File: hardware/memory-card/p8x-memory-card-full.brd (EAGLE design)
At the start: 160 x 100 mm, 30 parts, among them J1 FABC96R, U1 28C256, U2 62256, U3 74HCT245, U4 74HCT30, U5 74HCT138, U6 74HCT138, U7 74HCT00, U8 74HCT32, U9 74HCT08

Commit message: feat(hardware): use con-vg DIN 41612 footprints (MABC96R card / FABC96S backplane)
Replace the hand-rolled DIN96/DIN96C connector packages with the real Eagle
con-vg DIN 41612 footprints (geometry baked into the generator so it stays
self-contained): card edge = MABC96R (male right-angle), backplane = FABC96S
(female vertical) — both A/B/C @ 2.54mm, drill 0.9144, two M2.5 mounting holes
at y=+/-45. Card value -> MABC96R; pin->pad names unchanged (A1..C32) so the
netlist is intact.

con-vg centres the pad field on the element origin, so the backplane (hand-
placed/routed) was re-derived: slots dropped to y=54.6 to centre the pin field
on the 109mm board (pads now on-board), bus traces re-routed to the new A/B/C
columns (element at sx(i)-2.54). Cards auto-adapt via fp_box. All 8 boards
validate (0 errors).

Known: 3 placement-overlap WARNINGS on the backplane (power-LED resistor; CT2/RT1
clock terminators, both DNP) where the taller connector crowds the top/bottom
strips — to clear during the Fusion placement pass.

Co-Authored-By: Claude Opus 4.8 <noreply@anthropic.com>
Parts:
- J1: value FABC96R -> MABC96R; device p8x:DIN96C -> p8x:MABC96R
- moved J1 37.5 mm to (7.94, 49.6)

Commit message: feat(hardware): 100nF bypass caps to 0.1" lead pitch on all boards
The 100nF ceramic-disc decoupling/bypass caps used the shared C_DISC footprint
at 0.2" (5.08mm) lead spacing. The parts being sourced are 0.1" (2.54mm) pitch,
so retarget just those caps:

- Add a C_DISC1 footprint (pad 2 at y=-2.54) and a CAP1 device that reuses the
  CAP schematic symbol art but points at C_DISC1.
- Route the 100nF parts to CAP1: per-IC decoupling (CDn), the placement-flow
  copies, and the backplane per-slot caps C1-C10.
- Leave C_DISC (0.2") for the parts that still use it: the 1uF caps, the 150pF
  clock terminators (CT1/CT2), and the XTAL32 placeholder.

Regenerated all 8 boards (.sch/.brd/-full.brd) and the schematic PDFs; the
narrower pad field also relieves the backplane connector clearance. Validation:
0 errors on all boards.

Co-Authored-By: Claude Opus 4.8 <noreply@anthropic.com>
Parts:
- CD1, CD2, CD3, CD4, CD5, CD6, CD7, CD8, CD9: device p8x:C_DISC -> p8x:C_DISC1
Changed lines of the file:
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@@
 <attribute name="VALUE" x="17.87" y="92.66" size="1.778" layer="27" ratio="10"/>
 </element>
-<element name="CD1" library="p8x" package="C_DISC" value="100N" x="37.41" y="95.10" smashed="yes">
+<element name="CD1" library="p8x" package="C_DISC1" value="100N" x="37.41" y="95.10" smashed="yes">
 <attribute name="NAME" x="37.41" y="97.64" size="1.778" layer="25" ratio="10"/>
 <attribute name="VALUE" x="37.41" y="92.56" size="1.778" layer="27" ratio="10"/>
@@
 <attribute name="VALUE" x="41.71" y="92.66" size="1.778" layer="27" ratio="10"/>
 </element>
-<element name="CD2" library="p8x" package="C_DISC" value="100N" x="61.25" y="95.10" smashed="yes">
+<element name="CD2" library="p8x" package="C_DISC1" value="100N" x="61.25" y="95.10" smashed="yes">
 <attribute name="NAME" x="61.25" y="97.64" size="1.778" layer="25" ratio="10"/>
 <attribute name="VALUE" x="61.25" y="92.56" size="1.778" layer="27" ratio="10"/>
@@
 <attribute name="VALUE" x="65.55" y="92.66" size="1.778" layer="27" ratio="10"/>
 </element>
-<element name="CD3" library="p8x" package="C_DISC" value="100N" x="77.47" y="95.10" smashed="yes">
+<element name="CD3" library="p8x" package="C_DISC1" value="100N" x="77.47" y="95.10" smashed="yes">
 <attribute name="NAME" x="77.47" y="97.64" size="1.778" layer="25" ratio="10"/>
 <attribute name="VALUE" x="77.47" y="92.56" size="1.778" layer="27" ratio="10"/>
@@
 <attribute name="VALUE" x="81.77" y="92.66" size="1.778" layer="27" ratio="10"/>
 </element>
-<element name="CD4" library="p8x" package="C_DISC" value="100N" x="93.69" y="95.10" smashed="yes">
+<element name="CD4" library="p8x" package="C_DISC1" value="100N" x="93.69" y="95.10" smashed="yes">
 <attribute name="NAME" x="93.69" y="97.64" size="1.778" layer="25" ratio="10"/>
 <attribute name="VALUE" x="93.69" y="92.56" size="1.778" layer="27" ratio="10"/>
@@
 <attribute name="VALUE" x="97.99" y="92.66" size="1.778" layer="27" ratio="10"/>
 </element>
-<element name="CD5" library="p8x" package="C_DISC" value="100N" x="109.91" y="95.10" smashed="yes">
+<element name="CD5" library="p8x" package="C_DISC1" value="100N" x="109.91" y="95.10" smashed="yes">
 <attribute name="NAME" x="109.91" y="97.64" size="1.778" layer="25" ratio="10"/>
 <attribute name="VALUE" x="109.91" y="92.56" size="1.778" layer="27" ratio="10"/>
@@
 <attribute name="VALUE" x="114.21" y="92.66" size="1.778" layer="27" ratio="10"/>
 </element>
-<element name="CD6" library="p8x" package="C_DISC" value="100N" x="126.13" y="95.10" smashed="yes">
+<element name="CD6" library="p8x" package="C_DISC1" value="100N" x="126.13" y="95.10" smashed="yes">
 <attribute name="NAME" x="126.13" y="97.64" size="1.778" layer="25" ratio="10"/>
 <attribute name="VALUE" x="126.13" y="92.56" size="1.778" layer="27" ratio="10"/>
@@
 <attribute name="VALUE" x="130.43" y="92.66" size="1.778" layer="27" ratio="10"/>
 </element>
-<element name="CD7" library="p8x" package="C_DISC" value="100N" x="142.35" y="95.10" smashed="yes">
+<element name="CD7" library="p8x" package="C_DISC1" value="100N" x="142.35" y="95.10" smashed="yes">
 <attribute name="NAME" x="142.35" y="97.64" size="1.778" layer="25" ratio="10"/>
 <attribute name="VALUE" x="142.35" y="92.56" size="1.778" layer="27" ratio="10"/>
@@
 <attribute name="VALUE" x="146.65" y="92.66" size="1.778" layer="27" ratio="10"/>
 </element>
-<element name="CD8" library="p8x" package="C_DISC" value="100N" x="17.97" y="57.88" smashed="yes">
+<element name="CD8" library="p8x" package="C_DISC1" value="100N" x="17.97" y="57.88" smashed="yes">
 <attribute name="NAME" x="17.97" y="60.42" size="1.778" layer="25" ratio="10"/>
 <attribute name="VALUE" x="17.97" y="55.34" size="1.778" layer="27" ratio="10"/>
@@
 <attribute name="VALUE" x="22.27" y="55.44" size="1.778" layer="27" ratio="10"/>
 </element>
-<element name="CD9" library="p8x" package="C_DISC" value="100N" x="34.19" y="57.88" smashed="yes">
+<element name="CD9" library="p8x" package="C_DISC1" value="100N" x="34.19" y="57.88" smashed="yes">
 <attribute name="NAME" x="34.19" y="60.42" size="1.778" layer="25" ratio="10"/>
 <attribute name="VALUE" x="34.19" y="55.34" size="1.778" layer="27" ratio="10"/>

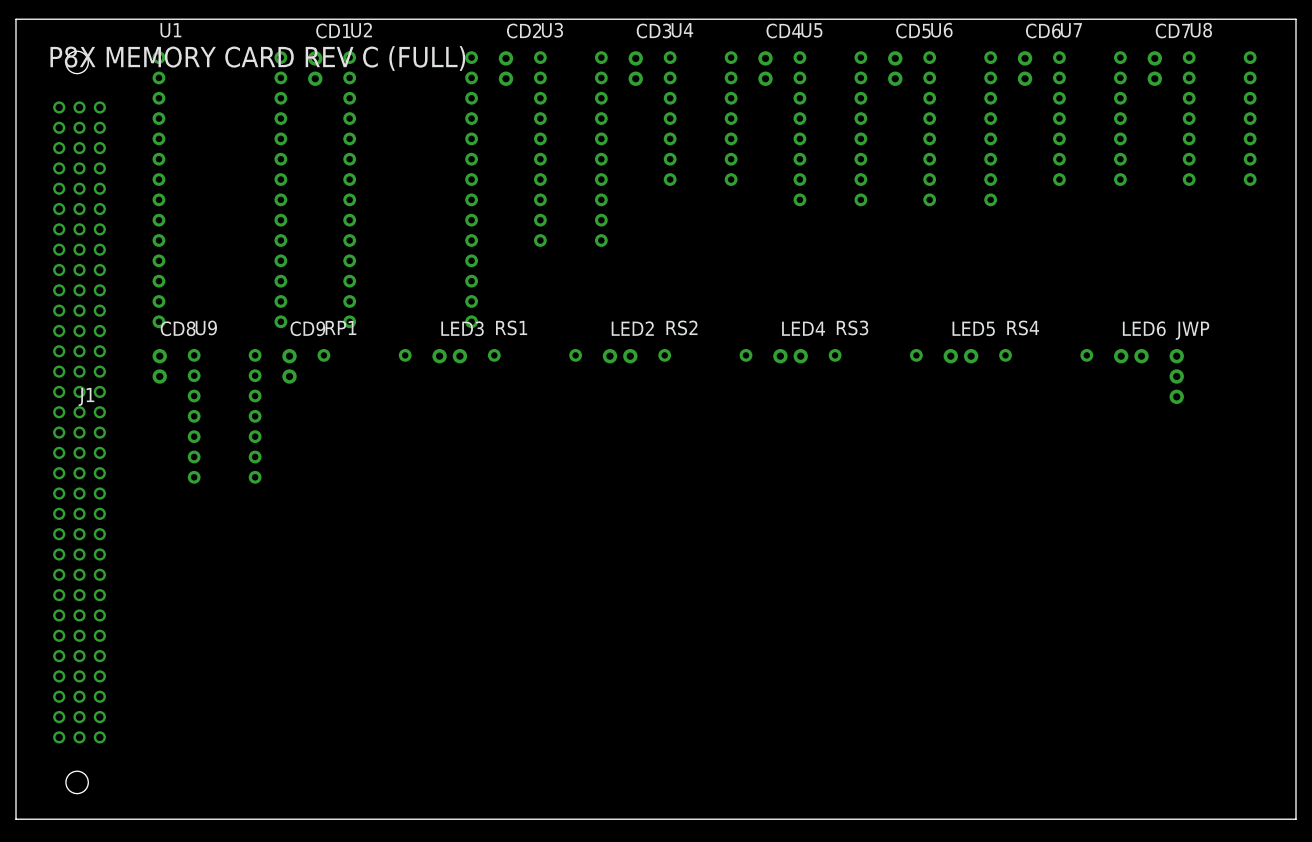
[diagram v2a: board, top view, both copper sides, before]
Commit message: feat(hardware): memory card rev D — 16K ROM + 48K RAM (2x 62256)
Shrink the ROM window to $0000-$3FFF (16K; 28C256 stays, low half addressed —
monitor+BASIC end at $3307) and grow RAM to 48K ($4000-$FEFF) with a second
62256 (U10) at $4000-$7FFF.

Decode now keys on A15+A14:
- ROM  U1  !CE = A15 OR A14            -> $0000-$3FFF   (spare U8 OR gate)
- RAM  U10 !CE = NAND(!A15, A14)        -> $4000-$7FFF  (spare U7 NAND gates)
- RAM  U2  !CE = NAND(A15, -IOPG)       -> $8000-$FEFF  (unchanged; I/O carve-out)

Reuses existing spare gates in U7/U8 — no added logic IC; the only new parts are
U10 + its 100nF. The memory card is the ONLY board that changes (backplane, CF,
I/O, control, regbank, ALU untouched). Emulator memory map updated to match.

No firmware/OS change: everything at $8000+ stays put, so $4000-$7FFF is simply
unused RAM for now. (This sets up a future lower OS load address to lift the
14-sector boot ceiling, but that's deferred.)

Test: emulator/test/test_ram48.asm (`make test-mem`) writes/reads $5000 to prove
the new bank is RAM. Full suite (ISA/CF/OS/BASIC/IO) still passes. Docs updated:
memory-card theory + README, cf-os design map, top-level README.

Co-Authored-By: Claude Opus 4.8 <noreply@anthropic.com>
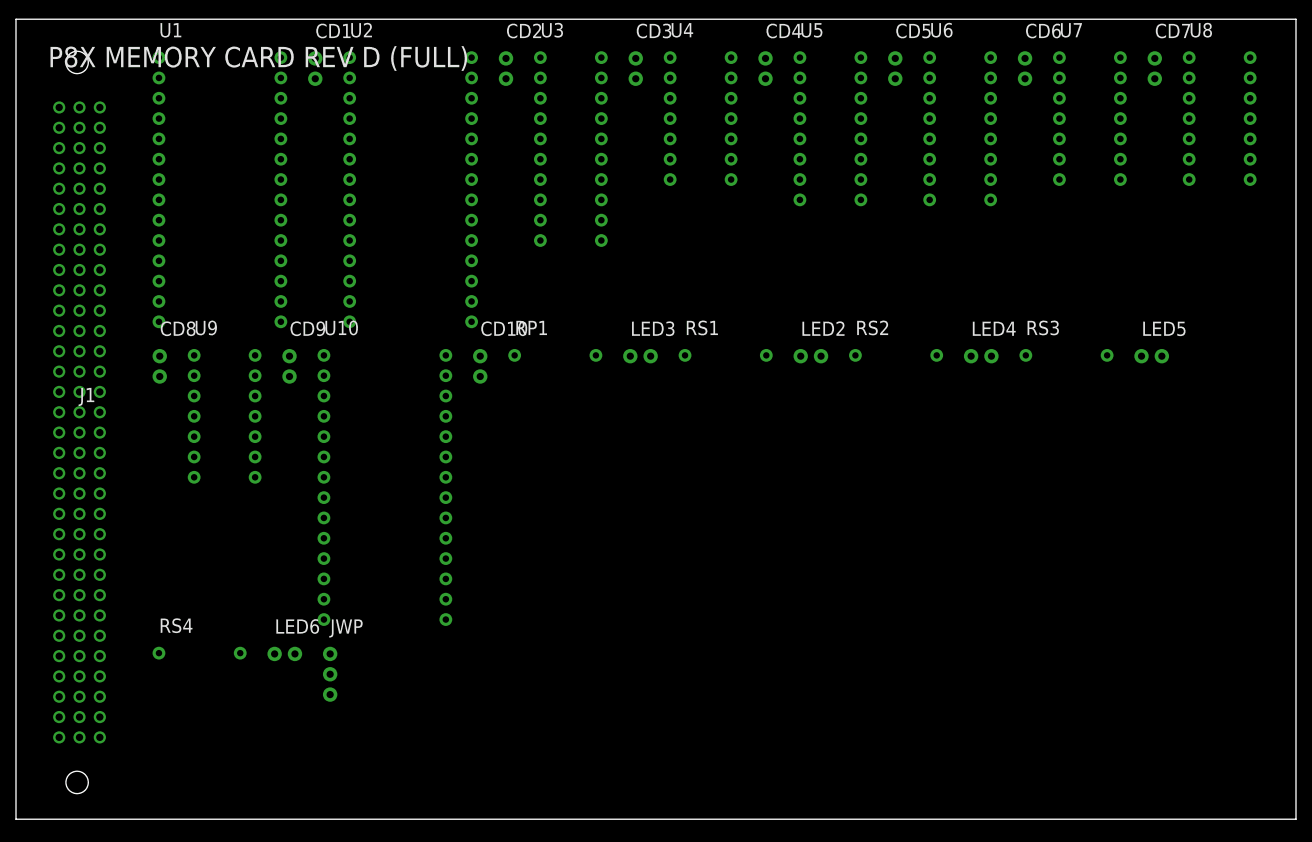
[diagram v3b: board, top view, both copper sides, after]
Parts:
- added CD10: 100N, p8x:C_DISC1
- added U10: 62256, p8x:DIP28W
- moved LED6 112.2 mm to (32.3, 20.7)
- moved JWP 112.2 mm to (39.3, 20.7)
- moved RS4 112.2 mm to (17.9, 20.8)
- moved LED2 23.8 mm to (98.1, 57.9)
- moved LED3 23.8 mm to (76.8, 57.9)
- moved LED4 23.8 mm to (119.4, 57.9)
- moved LED5 23.8 mm to (140.7, 57.9)
- moved RS2 23.8 mm to (104.9, 58.0)
- moved RS3 23.8 mm to (126.2, 58.0)
- moved RP1 23.8 mm to (62.3, 58.0)
- moved RS1 23.8 mm to (83.6, 58.0)
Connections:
- new net -RAM2CE: U10.20, U7.8
- new net A15N: U7.6, U7.9
- new net ROMCE: U1.20, U8.11, U8.9
- net -RD: now also U10.22
- net -WE: now also U10.27
- net A0: now also U10.10
- net A1: now also U10.9
- net A10: now also U10.21
- net A11: now also U10.23
- net A12: now also U10.2
- net A13: now also U10.26
- net A14: now also U10.1, U7.10, U8.13
- net A15: now also U7.4, U7.5, U8.12; no longer U1.20, U8.9
- net A2: now also U10.8
- net A3: now also U10.7
- net A4: now also U10.6
- net A5: now also U10.5
- net A6: now also U10.4
- net A7: now also U10.3
- net A8: now also U10.25
- net A9: now also U10.24
- net GND: now also CD10.2, U10.14; no longer U7.10, U7.4, U7.5, U7.9, U8.12, U8.13
- net MD0: now also U10.11
- net MD1: now also U10.12
- net MD2: now also U10.13
- net MD3: now also U10.15
- net MD4: now also U10.16
- net MD5: now also U10.17
- net MD6: now also U10.18
- net MD7: now also U10.19
- net VCC: now also CD10.1, U10.28
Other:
- board text added: "P8X MEMORY CARD REV D (FULL)"
- board text removed: "P8X MEMORY CARD REV C (FULL)"

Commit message: feat(hardware): RAM2 bank-activity LED on the memory card (rev D)
Add a yellow RAM2 LED (LED7 + RS5) that lights when the new $4000-$7FFF bank
(U10) is addressed. Driven by U7's last spare NAND wired as an inverter, which
flips -RAM2CE to active-high and sources the LED through RS5. It's a bank-select
indicator (not -BOE-gated like the ROM/RAM/RD/WR LEDs — that would need another
spare gate, and only one remained). Validation: 0 errors, 0 overlaps; full
emulator suite still passes. Docs: memory-card README + theory.

Co-Authored-By: Claude Opus 4.8 <noreply@anthropic.com>
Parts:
- added LED7: YEL, p8x:LED5
- added RS5: 1K, p8x:R_AXIAL
- moved JWP 21.3 mm to (60.6, 20.7)
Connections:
- new net LEDRA2: LED7.2, RS5.2
- new net RAM2ON: RS5.1, U7.11
- net -RAM2CE: now also U7.12, U7.13
- net GND: now also LED7.1; no longer U7.12, U7.13
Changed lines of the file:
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@@
 <attribute name="VALUE" x="32.33" y="18.12" size="1.778" layer="27" ratio="10"/>
 </element>
-<element name="JWP" library="p8x" package="HDR3" value="1x3" x="39.27" y="20.66" smashed="yes">
-<attribute name="NAME" x="39.27" y="23.20" size="1.778" layer="25" ratio="10"/>
-<attribute name="VALUE" x="39.27" y="18.12" size="1.778" layer="27" ratio="10"/>
+<element name="RS5" library="p8x" package="R_AXIAL" value="1K" x="39.17" y="20.76" smashed="yes">
+<attribute name="NAME" x="39.17" y="23.30" size="1.778" layer="25" ratio="10"/>
+<attribute name="VALUE" x="39.17" y="18.22" size="1.778" layer="27" ratio="10"/>
+</element>
+<element name="LED7" library="p8x" package="LED5" value="YEL" x="53.63" y="20.66" smashed="yes">
+<attribute name="NAME" x="53.63" y="23.20" size="1.778" layer="25" ratio="10"/>
+<attribute name="VALUE" x="53.63" y="18.12" size="1.778" layer="27" ratio="10"/>
+</element>
+<element name="JWP" library="p8x" package="HDR3" value="1x3" x="60.57" y="20.66" smashed="yes">
+<attribute name="NAME" x="60.57" y="23.20" size="1.778" layer="25" ratio="10"/>
+<attribute name="VALUE" x="60.57" y="18.12" size="1.778" layer="27" ratio="10"/>
 </element>
 </elements><signals>
@@
 <contactref element="U7" pad="8"/>
 <contactref element="U10" pad="20"/>
+<contactref element="U7" pad="12"/>
+<contactref element="U7" pad="13"/>
 </signal>
 <signal name="-RAMCE">
@@
 <contactref element="U5" pad="5"/>
 <contactref element="U6" pad="5"/>
-<contactref element="U7" pad="12"/>
-<contactref element="U7" pad="13"/>
 <contactref element="U9" pad="12"/>
 <contactref element="U9" pad="13"/>
 <contactref element="LED3" pad="1"/>
+<contactref element="LED7" pad="1"/>
 <contactref element="J1" pad="A31"/>
 <contactref element="J1" pad="A32"/>
@@
 <contactref element="LED4" pad="2"/>
 </signal>
+<signal name="LEDRA2">
+<contactref element="RS5" pad="2"/>
+<contactref element="LED7" pad="2"/>
+</signal>
 <signal name="LEDRD">
 <contactref element="RS3" pad="2"/>
@@
 <contactref element="U10" pad="19"/>
 </signal>
+<signal name="RAM2ON">
+<contactref element="U7" pad="11"/>
+<contactref element="RS5" pad="1"/>
+</signal>
 <signal name="RAMK">
